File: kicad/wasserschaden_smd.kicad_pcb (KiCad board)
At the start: 2 copper layers, 49.5 x 33 mm, 19 parts, among them J1 valve out, J2 12V in, J3 sense, U1 stepdown, U2 WeMos_mini, U3 DS18B20

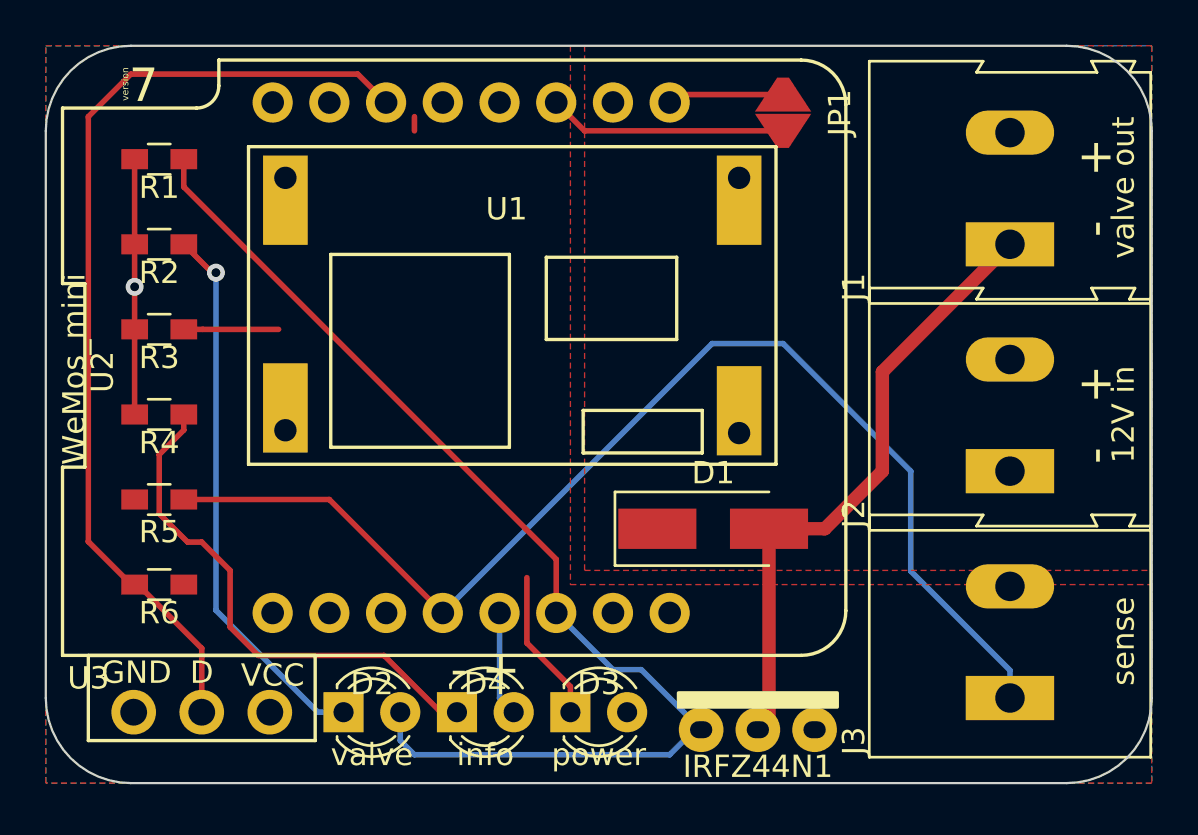
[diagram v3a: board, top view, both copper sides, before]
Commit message: fixed D3 in current pcb
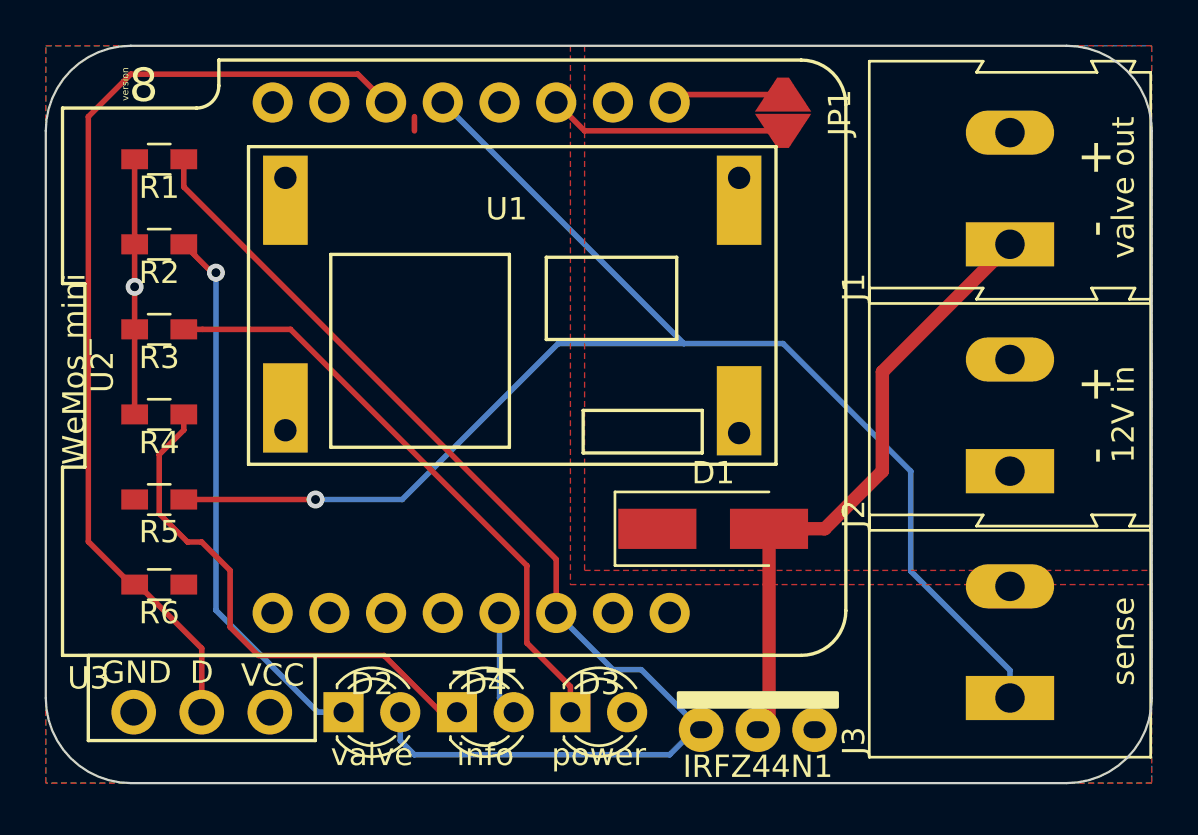
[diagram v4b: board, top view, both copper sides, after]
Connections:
- U2 pad 13: Net-(U2-Pad13) -> Net-(J3-Pad1)
- U2 pad 4: Net-(J3-Pad1) -> Net-(U2-Pad4)
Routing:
- net Net-(D3-Pad1): track 11.1 -> 27.1 mm
- net Net-(J3-Pad1): track 54.0 -> 65.1 mm, vias 0 -> 1
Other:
- board text added: "8"
- board text removed: "7"
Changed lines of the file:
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@@
-(kicad_pcb (version 20171130) (host pcbnew 5.0.1)
+(kicad_pcb (version 20171130) (host pcbnew 5.1.1)
   (general
     (thickness 1.6)
     (drawings 17)
-    (tracks 67)
+    (tracks 71)
     (zones 0)
     (modules 19)
@@
     (zone_45_only no)
     (trace_min 0.2)
-    (segment_width 0.2)
-    (edge_width 0.1)
     (via_size 0.8)
     (via_drill 0.4)
@@
     (uvia_min_size 0.2)
     (uvia_min_drill 0.1)
+    (edge_width 0.1)
+    (segment_width 0.2)
     (pcb_text_width 0.3)
     (pcb_text_size 1.5 1.5)
@@
   (net 15 "Net-(U2-Pad15)")
   (net 16 "Net-(U2-Pad3)")
-  (net 17 "Net-(U2-Pad13)")
-  (net 18 "Net-(U2-Pad12)")
-  (net 19 "Net-(U2-Pad10)")
-  (net 20 "Net-(U2-Pad7)")
-  (net 21 "Net-(U2-Pad8)")
+  (net 17 "Net-(U2-Pad12)")
+  (net 18 "Net-(U2-Pad10)")
+  (net 19 "Net-(U2-Pad7)")
+  (net 20 "Net-(U2-Pad8)")
+  (net 21 "Net-(U2-Pad4)")
   (net_class Default "This is the default net class."
     (clearance 0.2)
@@
     (add_net "Net-(U2-Pad10)")
     (add_net "Net-(U2-Pad12)")
-    (add_net "Net-(U2-Pad13)")
     (add_net "Net-(U2-Pad15)")
     (add_net "Net-(U2-Pad3)")
+    (add_net "Net-(U2-Pad4)")
     (add_net "Net-(U2-Pad7)")
     (add_net "Net-(U2-Pad8)")
@@
       (net 16 "Net-(U2-Pad3)"))
     (pad 13 thru_hole circle (at -1.27 -11.43) (size 1.8 1.8) (drill 1.016) (layers *.Cu *.Mask)
-      (net 17 "Net-(U2-Pad13)"))
-    (pad 4 thru_hole circle (at -1.27 11.43) (size 1.8 1.8) (drill 1.016) (layers *.Cu *.Mask)
       (net 10 "Net-(J3-Pad1)"))
+    (pad 4 thru_hole circle (at -1.27 11.43) (size 1.8 1.8) (drill 1.016) (layers *.Cu *.Mask)
+      (net 21 "Net-(U2-Pad4)"))
     (pad 12 thru_hole circle (at 1.27 -11.43) (size 1.8 1.8) (drill 1.016) (layers *.Cu *.Mask)
-      (net 18 "Net-(U2-Pad12)"))
+      (net 17 "Net-(U2-Pad12)"))
     (pad 5 thru_hole circle (at 1.27 11.43) (size 1.8 1.8) (drill 1.016) (layers *.Cu *.Mask)
       (net 8 "Net-(D4-Pad2)"))
@@
       (net 3 "Net-(D2-Pad2)"))
     (pad 10 thru_hole circle (at 6.35 -11.43) (size 1.8 1.8) (drill 1.016) (layers *.Cu *.Mask)
-      (net 19 "Net-(U2-Pad10)"))
+      (net 18 "Net-(U2-Pad10)"))
     (pad 7 thru_hole circle (at 6.35 11.43) (size 1.8 1.8) (drill 1.016) (layers *.Cu *.Mask)
-      (net 20 "Net-(U2-Pad7)"))
+      (net 19 "Net-(U2-Pad7)"))
     (pad 9 thru_hole circle (at 8.89 -11.43) (size 1.8 1.8) (drill 1.016) (layers *.Cu *.Mask)
       (net 12 "Net-(JP1-Pad2)"))
     (pad 8 thru_hole circle (at 8.89 11.43) (size 1.8 1.8) (drill 1.016) (layers *.Cu *.Mask)
-      (net 21 "Net-(U2-Pad8)"))
+      (net 20 "Net-(U2-Pad8)"))
     (model ${KIPRJMOD}/3dshapes/wemos_d1_mini.3dshapes/d1_mini_shield.wrl
       (offset (xyz -17.89999973116897 -12.79999980776329 5.099999923405687))
@@
     (effects (font (size 1 1) (thickness 0.2)))
   )
-  (gr_text 7 (at 144.78 55.245 90) (layer B.SilkS)
+  (gr_text 8 (at 144.78 55.245 90) (layer B.SilkS)
     (effects (font (size 40 33) (thickness 6)) (justify mirror))
   )
-  (gr_text 7 (at 122.4915 41.148) (layer F.SilkS)
+  (gr_text 8 (at 122.4915 41.148) (layer F.SilkS)
     (effects (font (size 1.5 1.5) (thickness 0.3)))
   )
@@
   (segment (start 124.46 63.67) (end 124.29 63.5) (width 0.25) (layer F.Cu) (net 5))
   (segment (start 134.62 42.543) (end 134.62 43.18) (width 0.25) (layer F.Cu) (net 5))
-  (segment (start 128.537002 52.07) (end 125.14 52.07) (width 0.25) (layer F.Cu) (net 6))
   (segment (start 125.14 52.07) (end 124.29 52.07) (width 0.25) (layer F.Cu) (net 6))
-  (segment (start 139.655001 66.115001) (end 139.655001 63.187999) (width 0.25) (layer F.Cu) (net 6))
-  (segment (start 141.605 68.065) (end 139.655001 66.115001) (width 0.25) (layer F.Cu) (net 6))
+  (segment (start 129.07 52.07) (end 125.14 52.07) (width 0.25) (layer F.Cu) (net 6))
+  (segment (start 139.655001 62.655001) (end 129.07 52.07) (width 0.25) (layer F.Cu) (net 6))
+  (segment (start 139.655001 66.115001) (end 139.655001 62.655001) (width 0.25) (layer F.Cu) (net 6))
   (segment (start 141.605 69.215) (end 141.605 68.065) (width 0.25) (layer F.Cu) (net 6))
+  (segment (start 141.605 68.065) (end 139.655001 66.115001) (width 0.25) (layer F.Cu) (net 6))
   (segment (start 124.46 61.595) (end 123.19 60.325) (width 0.25) (layer F.Cu) (net 7))
   (segment (start 124.29 56.58) (end 124.29 55.88) (width 0.25) (layer F.Cu) (net 7))
@@
   (segment (start 122.09 50.165) (end 122.09 55.88) (width 0.25) (layer F.Cu) (net 9))
   (via (at 122.09 50.165) (size 0.8) (drill 0.4) (layers F.Cu B.Cu) (net 9))
-  (segment (start 130.81 59.69) (end 135.89 64.77) (width 0.25) (layer F.Cu) (net 10))
-  (segment (start 124.29 59.69) (end 130.81 59.69) (width 0.25) (layer F.Cu) (net 10))
-  (segment (start 161.29 67.34) (end 161.29 68.58) (width 0.25) (layer B.Cu) (net 10))
-  (segment (start 156.845 58.42) (end 156.845 62.895) (width 0.25) (layer B.Cu) (net 10))
   (segment (start 156.845 62.895) (end 161.29 67.34) (width 0.25) (layer B.Cu) (net 10))
+  (segment (start 156.845 58.42) (end 156.845 62.895) (width 0.25) (layer B.Cu) (net 10))
   (segment (start 151.13 52.705) (end 156.845 58.42) (width 0.25) (layer B.Cu) (net 10))
-  (segment (start 135.89 64.77) (end 147.955 52.705) (width 0.25) (layer B.Cu) (net 10))
-  (segment (start 147.955 52.705) (end 151.13 52.705) (width 0.25) (layer B.Cu) (net 10))
+  (segment (start 161.29 67.34) (end 161.29 68.58) (width 0.25) (layer B.Cu) (net 10))
+  (segment (start 135.89 41.91) (end 146.685 52.705) (width 0.25) (layer B.Cu) (net 10))
+  (segment (start 146.685 52.705) (end 151.13 52.705) (width 0.25) (layer B.Cu) (net 10))
+  (via (at 130.19 59.69) (size 0.8) (drill 0.4) (layers F.Cu B.Cu) (net 10))
+  (segment (start 141.061998 52.705) (end 134.076998 59.69) (width 0.25) (layer B.Cu) (net 10))
+  (segment (start 146.685 52.705) (end 141.061998 52.705) (width 0.25) (layer B.Cu) (net 10))
+  (segment (start 124.29 59.69) (end 130.19 59.69) (width 0.25) (layer F.Cu) (net 10))
+  (segment (start 134.076998 59.69) (end 130.19 59.69) (width 0.25) (layer B.Cu) (net 10))
   (segment (start 142.24 43.18) (end 140.97 41.91) (width 0.25) (layer F.Cu) (net 11))
   (segment (start 151.13 43.18) (end 142.24 43.18) (width 0.25) (layer F.Cu) (net 11))
